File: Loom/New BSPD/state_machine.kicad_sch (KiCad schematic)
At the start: 8 parts, among them U1 4011, U10 4011, U12 4011, U14 4023, U15 4011, U16 4011, U5 4011, U7 74LS573

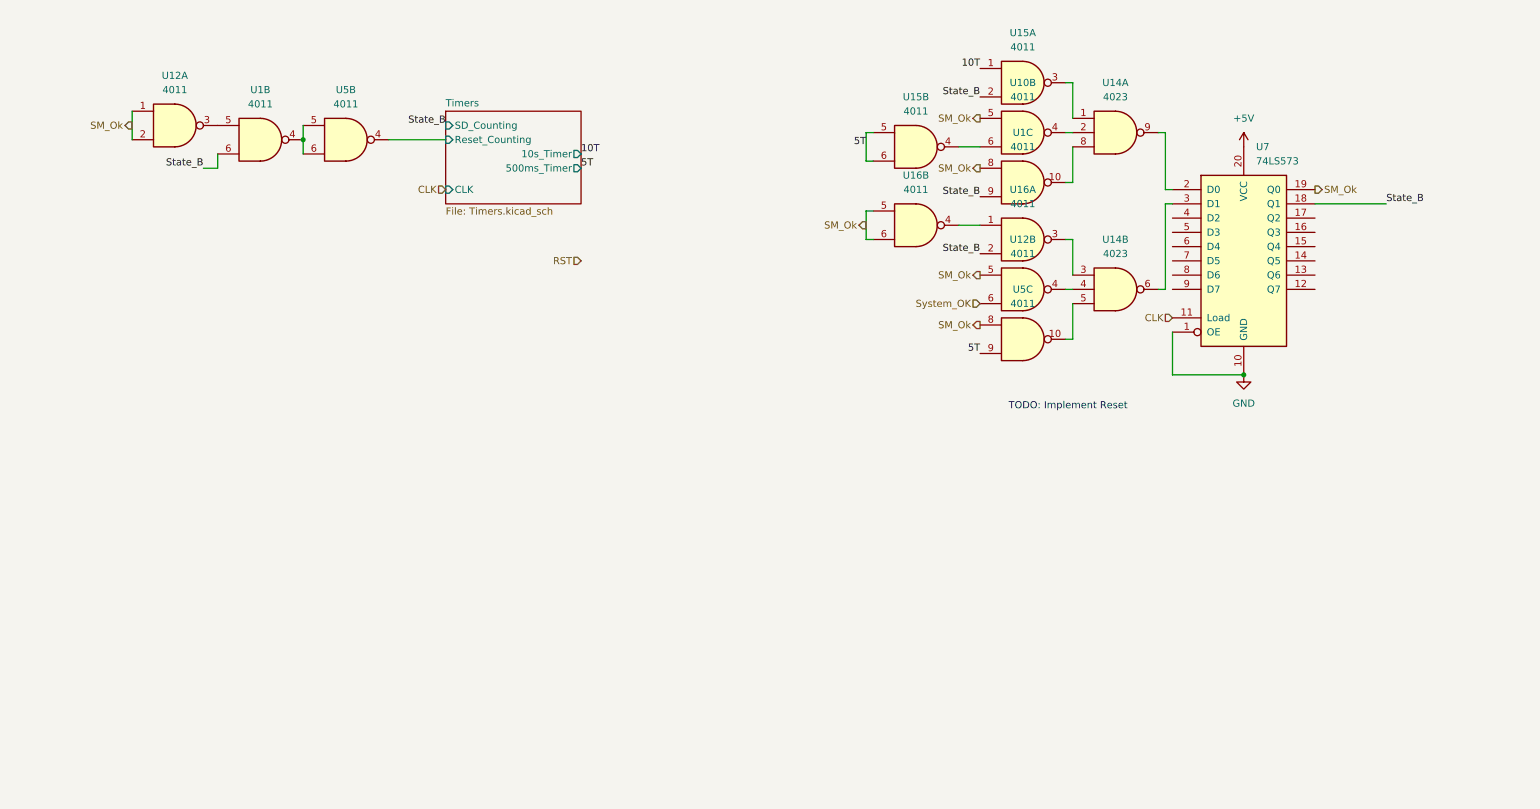
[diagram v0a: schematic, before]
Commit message: Fix BSPD Timing
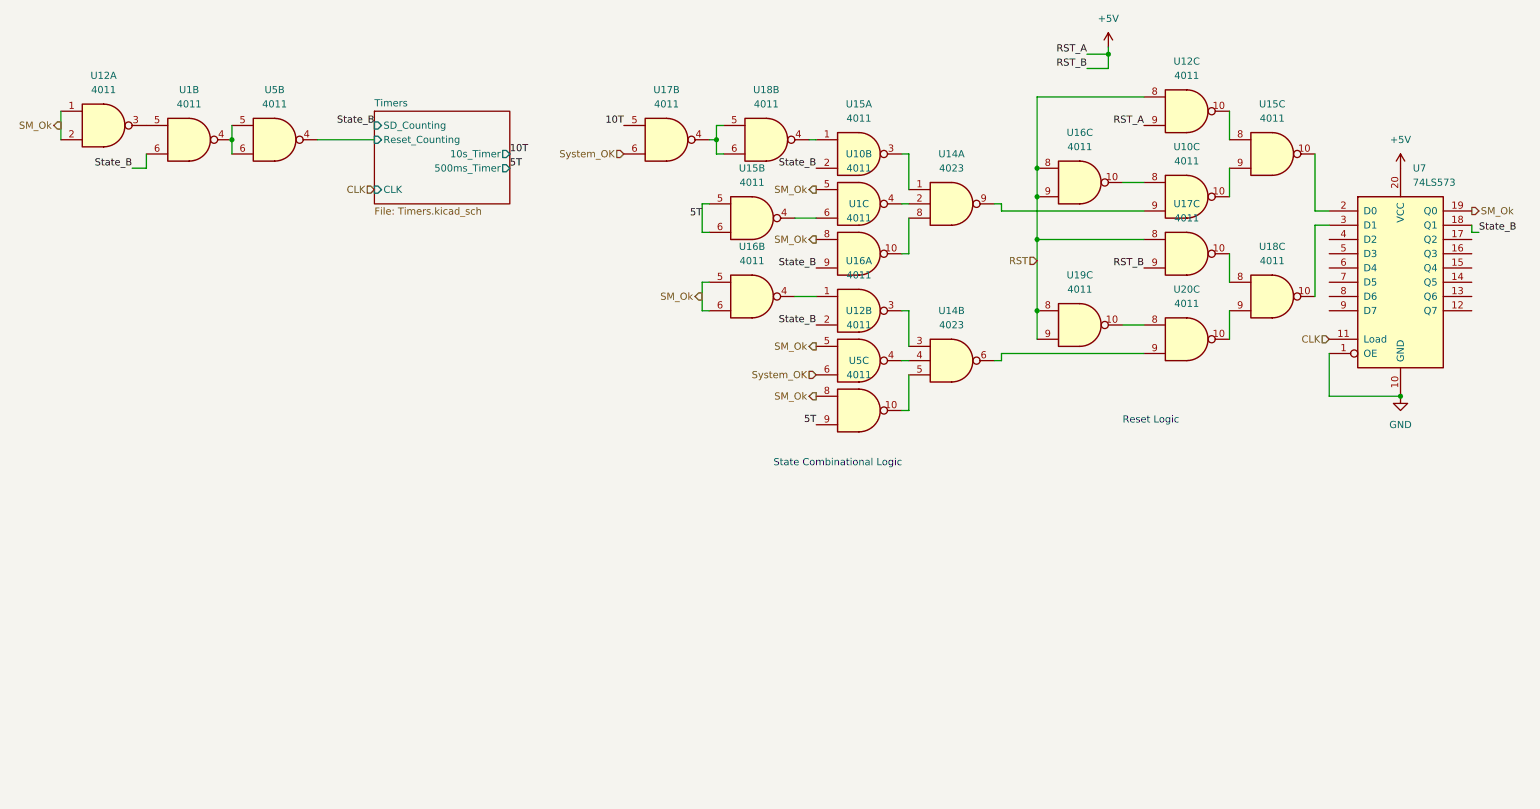
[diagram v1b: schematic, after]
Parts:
- added unit 3 of U10
- added unit 3 of U12
- added unit 3 of U15
- added unit 3 of U16
- added U17, U18, U19, U20: 4011, symbol 4xxx:4011
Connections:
- net +5V: now also U12.9, U17.9
- net 10T: now also U17.5; no longer U15.1
- net RST: now also U12.8, U16.8, U16.9, U17.8, U19.8, U19.9
- net System_OK: now also U17.6
- net at U7.2 (D0): now also U15.10; no longer U14.9
- net at U7.3 (D1): now also U18.10; no longer U14.6
- new net: U10.8, U16.10
- new net: U12.10, U15.8
- new net: U10.10, U15.9
- new net: U15.1, U18.4
- new net: U17.4, U18.5, U18.6
- new net: U19.10, U20.8
- new net: U10.9, U14.9
- new net: U17.10, U18.8
- new net: U18.9, U20.10
- new net: U14.6, U20.9
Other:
- note added: "Reset Logic"
- note added: "State Combinational Logic"
- note removed: "TODO: Implement Reset"
- moved on the sheet: U10B, U12A, U12B, U14A, U14B, U15A, U15B, U16A, U16B, U1B, U1C, U5B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

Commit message: Complete BSPD Schematic
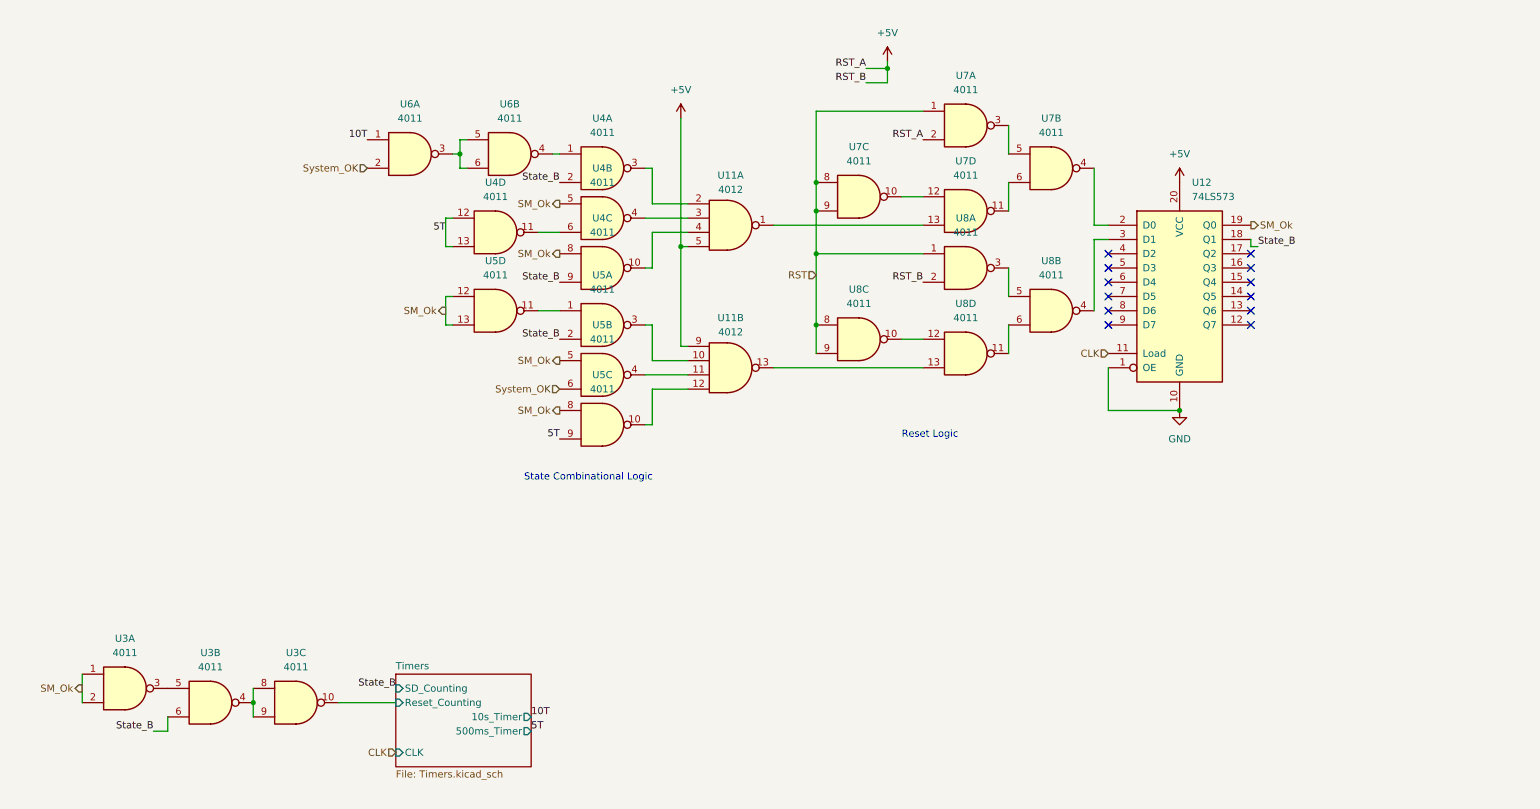
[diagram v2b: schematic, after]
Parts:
- removed U14: 4023, symbol 4xxx:4023
- added U11: 4012, symbol 4xxx:4012
- renumbered U7 to U12, U1 to U3, U12 to U3, U5 to U3, U1 to U4, U15 to U4, U10 to U4, U16 to U5, U12 to U5, U18 to U6, U17 to U6, U16 to U7, U15 to U7, U10 to U7, U12 to U7, U19 to U8, U17 to U8, U20 to U8, U18 to U8
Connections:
- net +5V: now also U7.2, U8.2, U11.5, U11.9; no longer U7.9, U8.9
- net 10T: now also U6.1; no longer U6.5
- net 5T: now also U4.12, U4.13; no longer U4.5, U4.6
- net RST: now also U7.1, U8.1; no longer U7.8, U8.8
- net SM_Ok: now also U5.12, U5.13; no longer U5.5, U5.6
- net System_OK: now also U6.2; no longer U6.6
- net Timers/Reset_Counting: now also U3.10; no longer U3.4
- net at U5.1: now also U5.11; no longer U5.4
- net at U5.3: now also U11.10
- net at U7.10: now also U7.12; no longer U7.8
- net at U12.2 (D0): now also U7.4; no longer U7.10
- net at U4.10: now also U11.4
- net at U6.5, U6.6: now also U6.3; no longer U6.4
- net at U8.10: now also U8.12; no longer U8.8
- net at U4.3: now also U11.2
- net at U4.4: now also U11.3
- net at U5.4: now also U11.11
- net at U12.3 (D1): now also U8.4; no longer U8.10
- net at U4.6: now also U4.11; no longer U4.4
- net at U5.10: now also U11.12
- new net: U7.3, U7.5
- new net: U7.11, U7.6
- new net: U11.1, U7.13
- new net: U3.4, U3.8, U3.9
- new net: U8.3, U8.5
- new net: U8.11, U8.6
- new net: U11.13, U8.13
- no-connect marks 0 -> 12
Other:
- moved on the sheet: U12, U3A, U3B, U3C, U4A, U4B, U4C, U4D, U5A, U5B, U5C, U5D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

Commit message: Complete Schematic, Footprint Assignment, Start PCB Design
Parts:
- U11, U3, U4, U5, U6, U7, U8: footprint (none) -> Package_DIP:DIP-14_W7.62mm_Socket
- U12: footprint (none) -> Package_DIP:DIP-20_W7.62mm_Socket
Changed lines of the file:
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@@
       (effects (font (size 1.27 1.27)))
     )
-    (property "Footprint" "" (at 120.65 68.58 0)
+    (property "Footprint" "Package_DIP:DIP-14_W7.62mm_Socket" (at 120.65 68.58 0)
       (effects (font (size 1.27 1.27)) hide)
     )
@@
       (effects (font (size 1.27 1.27)))
     )
-    (property "Footprint" "" (at 166.37 45.72 0)
+    (property "Footprint" "Package_DIP:DIP-14_W7.62mm_Socket" (at 166.37 45.72 0)
       (effects (font (size 1.27 1.27)) hide)
     )
@@
       (effects (font (size 1.27 1.27)))
     )
-    (property "Footprint" "" (at 200.66 40.64 0)
+    (property "Footprint" "Package_DIP:DIP-14_W7.62mm_Socket" (at 200.66 40.64 0)
       (effects (font (size 1.27 1.27)) hide)
     )
@@
       (effects (font (size 1.27 1.27)))
     )
-    (property "Footprint" "" (at 143.51 50.8 0)
+    (property "Footprint" "Package_DIP:DIP-14_W7.62mm_Socket" (at 143.51 50.8 0)
       (effects (font (size 1.27 1.27)) hide)
     )
@@
       (effects (font (size 1.27 1.27)))
     )
-    (property "Footprint" "" (at 50.8 135.89 0)
+    (property "Footprint" "Package_DIP:DIP-14_W7.62mm_Socket" (at 50.8 135.89 0)
       (effects (font (size 1.27 1.27)) hide)
     )
@@
       (effects (font (size 1.27 1.27)))
     )
-    (property "Footprint" "" (at 120.65 58.42 0)
+    (property "Footprint" "Package_DIP:DIP-14_W7.62mm_Socket" (at 120.65 58.42 0)
       (effects (font (size 1.27 1.27)) hide)
     )
@@
       (effects (font (size 1.27 1.27)))
     )
-    (property "Footprint" "" (at 104.14 38.1 0)
+    (property "Footprint" "Package_DIP:DIP-14_W7.62mm_Socket" (at 104.14 38.1 0)
       (effects (font (size 1.27 1.27)) hide)
     )
@@
       (effects (font (size 1.27 1.27)))
     )
-    (property "Footprint" "" (at 166.37 71.12 0)
+    (property "Footprint" "Package_DIP:DIP-14_W7.62mm_Socket" (at 166.37 71.12 0)
       (effects (font (size 1.27 1.27)) hide)
     )
@@
       (effects (font (size 1.27 1.27)))
     )
-    (property "Footprint" "" (at 185.42 48.26 0)
+    (property "Footprint" "Package_DIP:DIP-14_W7.62mm_Socket" (at 185.42 48.26 0)
       (effects (font (size 1.27 1.27)) hide)
     )
@@
       (effects (font (size 1.27 1.27)))
     )
-    (property "Footprint" "" (at 120.65 77.47 0)
+    (property "Footprint" "Package_DIP:DIP-14_W7.62mm_Socket" (at 120.65 77.47 0)
       (effects (font (size 1.27 1.27)) hide)
     )
@@
       (effects (font (size 1.27 1.27)))
     )
-    (property "Footprint" "" (at 101.6 66.04 0)
+    (property "Footprint" "Package_DIP:DIP-14_W7.62mm_Socket" (at 101.6 66.04 0)
       (effects (font (size 1.27 1.27)) hide)
     )
@@
       (effects (font (size 1.27 1.27)))
     )
-    (property "Footprint" "" (at 185.42 33.02 0)
+    (property "Footprint" "Package_DIP:DIP-14_W7.62mm_Socket" (at 185.42 33.02 0)
       (effects (font (size 1.27 1.27)) hide)
     )
@@
       (effects (font (size 1.27 1.27)))
     )
-    (property "Footprint" "" (at 185.42 58.42 0)
+    (property "Footprint" "Package_DIP:DIP-14_W7.62mm_Socket" (at 185.42 58.42 0)
       (effects (font (size 1.27 1.27)) hide)
     )
@@
       (effects (font (size 1.27 1.27)) (justify left))
     )
-    (property "Footprint" "" (at 223.52 63.5 0)
+    (property "Footprint" "Package_DIP:DIP-20_W7.62mm_Socket" (at 223.52 63.5 0)
       (effects (font (size 1.27 1.27)) hide)
     )
@@
       (effects (font (size 1.27 1.27)))
     )
-    (property "Footprint" "" (at 120.65 40.64 0)
+    (property "Footprint" "Package_DIP:DIP-14_W7.62mm_Socket" (at 120.65 40.64 0)
       (effects (font (size 1.27 1.27)) hide)
     )
@@
       (effects (font (size 1.27 1.27)))
     )
-    (property "Footprint" "" (at 120.65 49.53 0)
+    (property "Footprint" "Package_DIP:DIP-14_W7.62mm_Socket" (at 120.65 49.53 0)
       (effects (font (size 1.27 1.27)) hide)
     )
@@
       (effects (font (size 1.27 1.27)))
     )
-    (property "Footprint" "" (at 35.56 133.35 0)
+    (property "Footprint" "Package_DIP:DIP-14_W7.62mm_Socket" (at 35.56 133.35 0)
       (effects (font (size 1.27 1.27)) hide)
     )
@@
       (effects (font (size 1.27 1.27)))
     )
-    (property "Footprint" "" (at 185.42 73.66 0)
+    (property "Footprint" "Package_DIP:DIP-14_W7.62mm_Socket" (at 185.42 73.66 0)
       (effects (font (size 1.27 1.27)) hide)
     )
@@
       (effects (font (size 1.27 1.27)))
     )
-    (property "Footprint" "" (at 86.36 38.1 0)
+    (property "Footprint" "Package_DIP:DIP-14_W7.62mm_Socket" (at 86.36 38.1 0)
       (effects (font (size 1.27 1.27)) hide)
     )
@@
       (effects (font (size 1.27 1.27)))
     )
-    (property "Footprint" "" (at 120.65 86.36 0)
+    (property "Footprint" "Package_DIP:DIP-14_W7.62mm_Socket" (at 120.65 86.36 0)
       (effects (font (size 1.27 1.27)) hide)
     )
@@
       (effects (font (size 1.27 1.27)))
     )
-    (property "Footprint" "" (at 143.51 76.2 0)
+    (property "Footprint" "Package_DIP:DIP-14_W7.62mm_Socket" (at 143.51 76.2 0)
       (effects (font (size 1.27 1.27)) hide)
     )
@@
       (effects (font (size 1.27 1.27)))
     )
-    (property "Footprint" "" (at 66.04 135.89 0)
+    (property "Footprint" "Package_DIP:DIP-14_W7.62mm_Socket" (at 66.04 135.89 0)
       (effects (font (size 1.27 1.27)) hide)
     )
@@
       (effects (font (size 1.27 1.27)))
     )
-    (property "Footprint" "" (at 200.66 66.04 0)
+    (property "Footprint" "Package_DIP:DIP-14_W7.62mm_Socket" (at 200.66 66.04 0)
       (effects (font (size 1.27 1.27)) hide)
     )
@@
       (effects (font (size 1.27 1.27)))
     )
-    (property "Footprint" "" (at 101.6 52.07 0)
-      (effects (font (size 1.27 1.27)) hide)
-    )
+    (property "Footprint" "Package_DIP:DIP-14_W7.62mm_Socket" (at 101.6 52.07 0)
+      (effects (font (size 1.27 1.27)) hide)
+    )

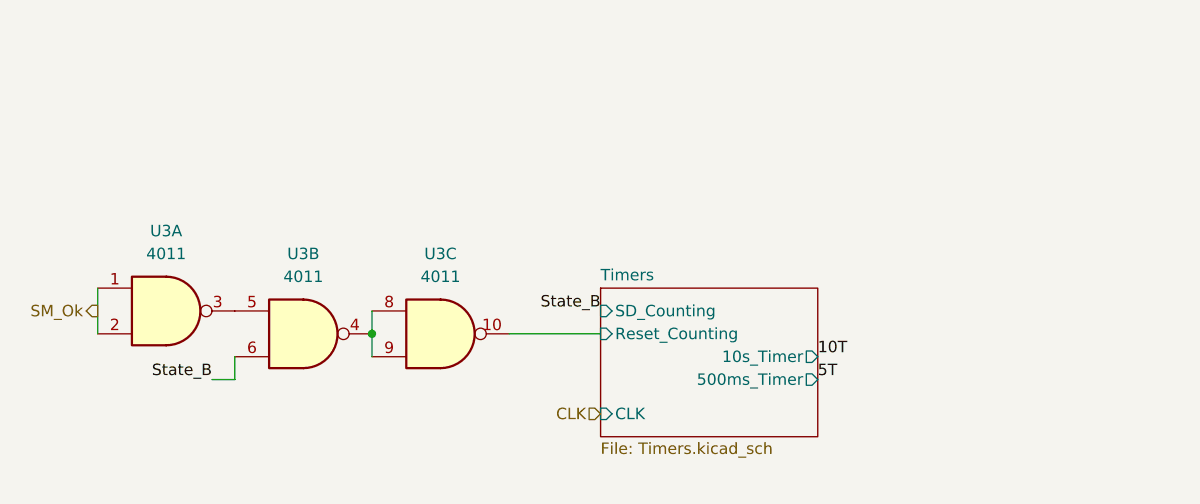
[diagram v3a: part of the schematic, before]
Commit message: Fix bug in state machine counters
Realised that the reset counter would count even in an error
condition, meaning that if 10 seconds pass after shutdown, it will
turn back on instantly after the system is ok.

Fixed by making the reset counter only count if system_ok is high
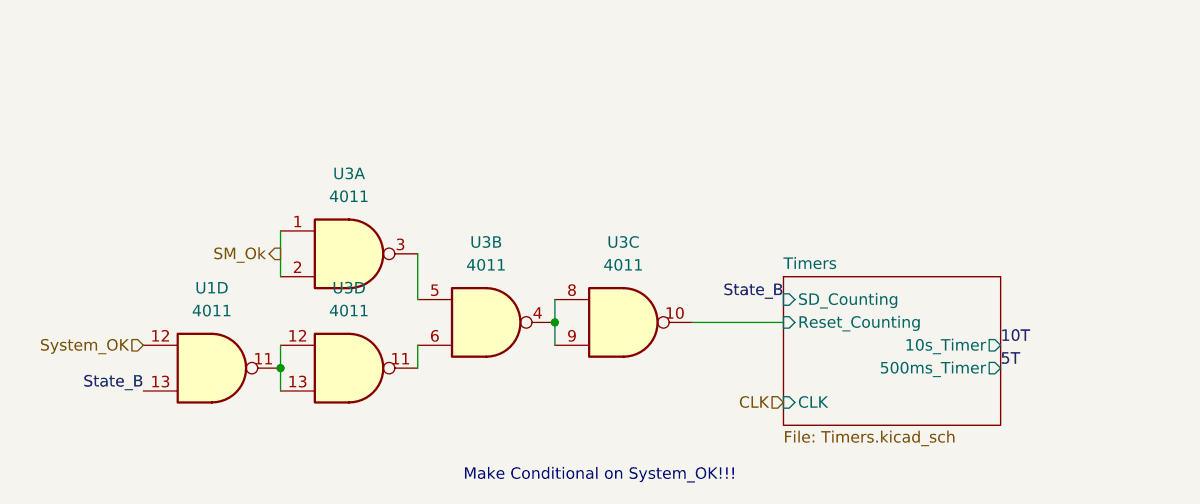
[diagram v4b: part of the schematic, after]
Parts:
- added U1: 4011, Package_DIP:DIP-14_W7.62mm_Socket, symbol 4xxx:4011
- added unit 4 of U3
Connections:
- net State_B: now also U1.13; no longer U3.6
- net System_OK: now also U1.12
- new net: U3.11, U3.6
- new net: U1.11, U3.12, U3.13
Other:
- note added: "Make Conditional on System_OK!!!"
- moved on the sheet: U3A, U3B, U3C
